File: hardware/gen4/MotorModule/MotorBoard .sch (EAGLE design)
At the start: 64 parts, among them IC1 XMEGA16A4A, M1O1 TEST_PT, M1O2 TEST_PT, M1O3 TEST_PT

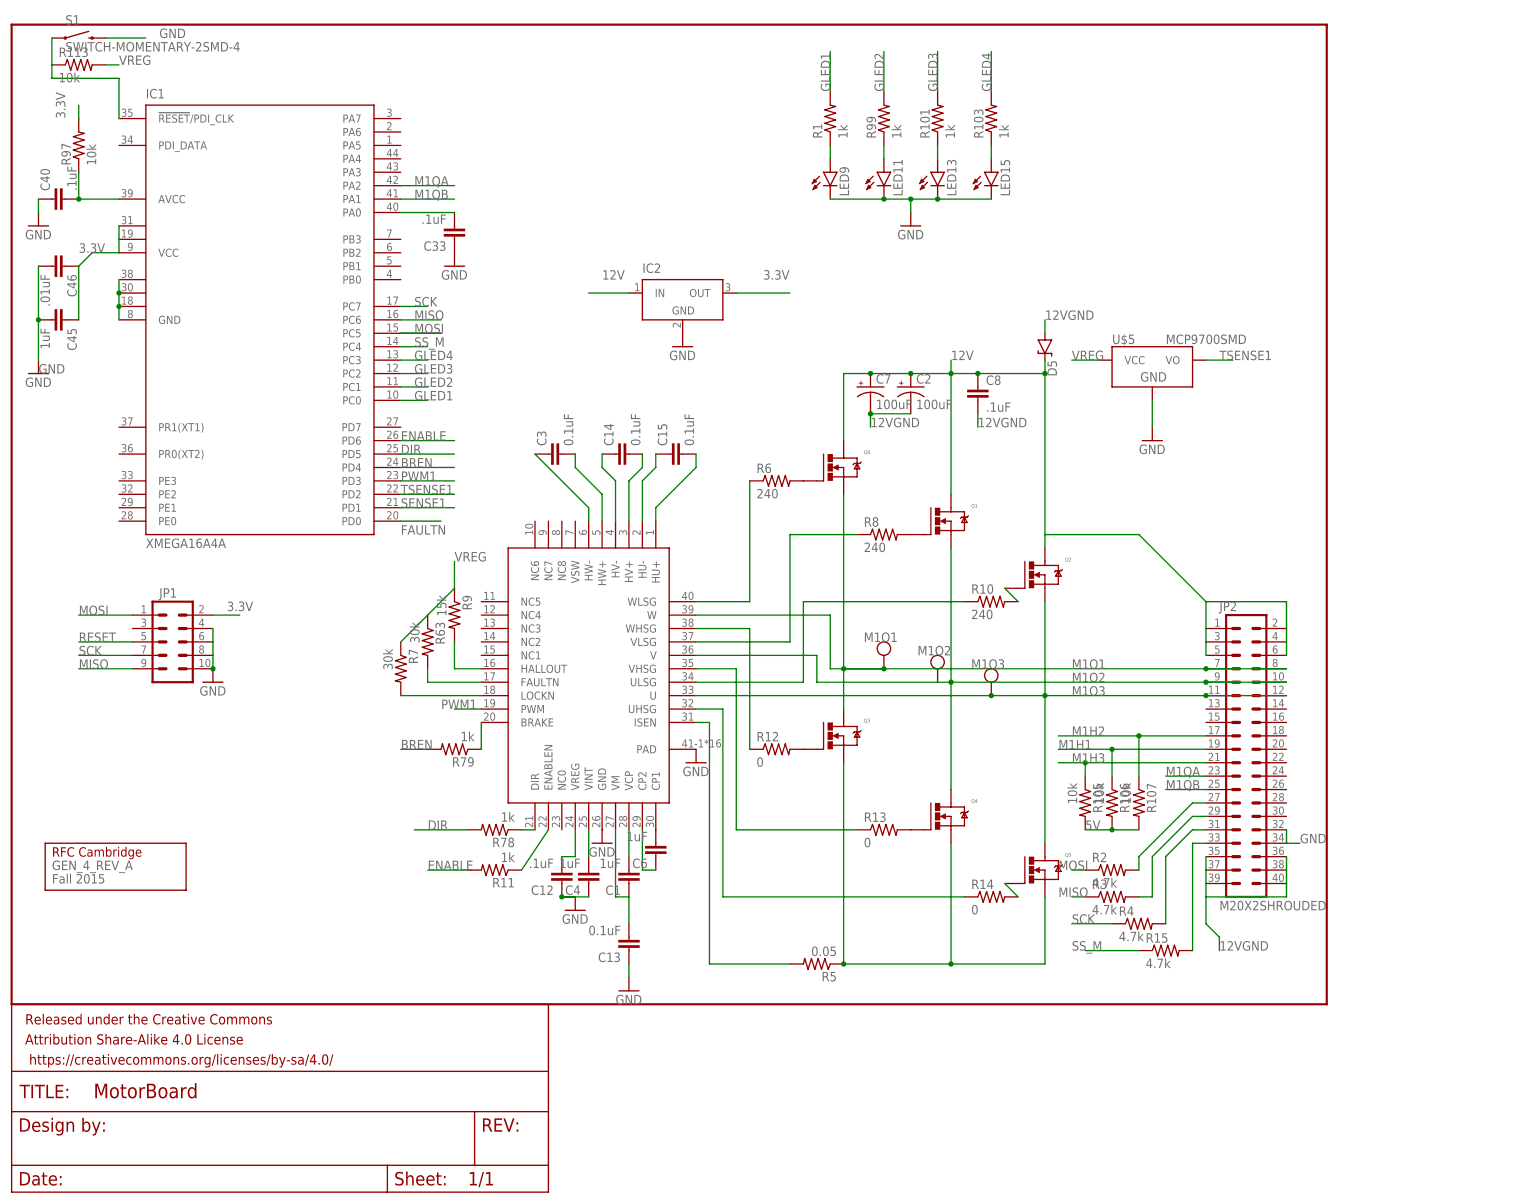
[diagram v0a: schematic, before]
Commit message: mother and motor board touchups
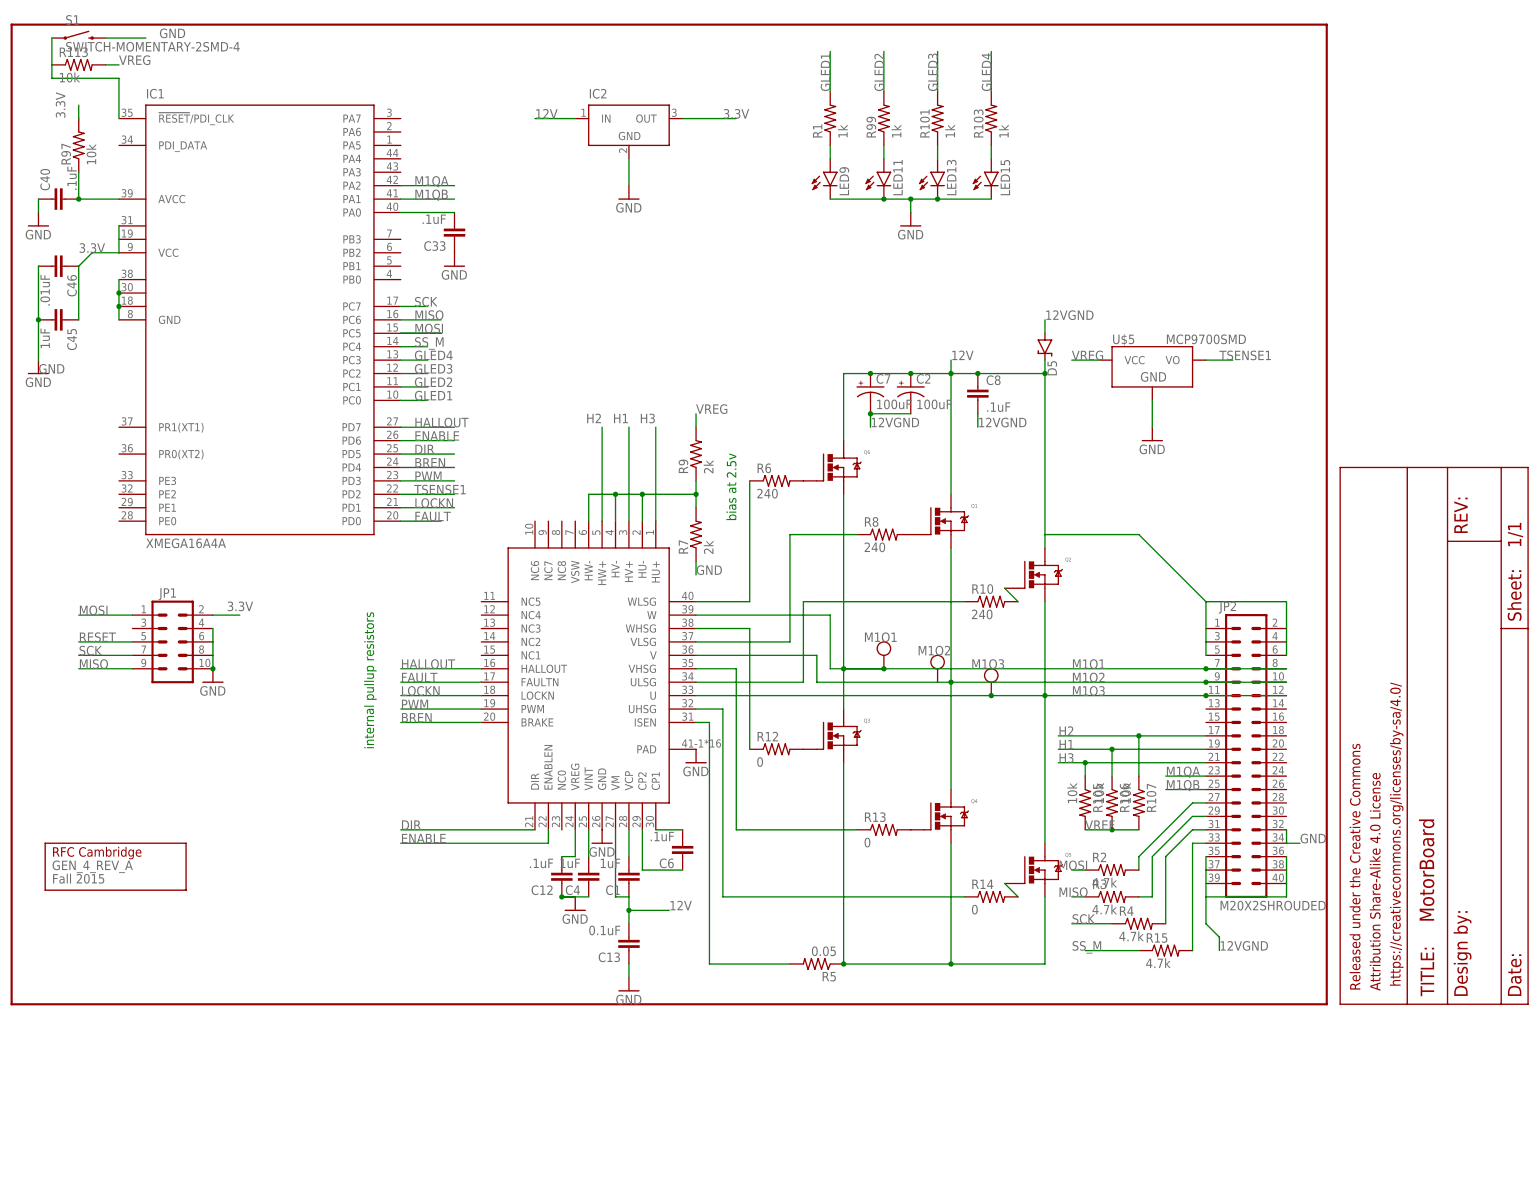
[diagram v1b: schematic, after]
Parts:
- removed C14, C15, C3: 0.1uF, SparkFun-Passives:CAP0805
- removed R11, R78, R79: 1k, SparkFun-Resistors:RESISTOR0805-RES
- removed R63: 30k, SparkFun-Resistors:RESISTOR0805-RES
- C6: value 1uF -> .1uF
- R7: value 30k -> 2k
- R9: value 15k -> 2k
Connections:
- net 5V renamed VREF
- net PWM1 renamed PWM
- removed net FAULT1: IC1.PD0
- removed net M1H1: JP2.19, R106.1
- removed net M1H2: JP2.17, R107.1
- removed net M1H3: JP2.21, R105.1
- removed net N$22: C3.1, U$1.HW-
- removed net N$23: R79.1, U$1.BRAKE
- removed net N$24: R7.2, U$1.LOCKN
- removed net N$25: C3.2, U$1.HW+
- removed net N$26: C14.1, U$1.HV-
- removed net N$27: C14.2, U$1.HV+
- removed net N$28: R63.2, U$1.FAULTN
- removed net N$30: C15.2, U$1.HU+
- removed net N$31: R9.2, U$1.HALLOUT
- removed net N$32: R11.1, U$1.ENABLEN
- removed net N$98: R78.1, U$1.DIR
- removed net SENSE1: IC1.PD1
- new net FAULT: IC1.PD0, U$1.FAULTN
- new net H1: JP2.19, R106.1, U$1.HV+
- new net H2: JP2.17, R107.1, U$1.HW+
- new net H3: JP2.21, R105.1, U$1.HU+
- new net HALLOUT: IC1.PD7, U$1.HALLOUT
- new net LOCKN: IC1.PD1, U$1.LOCKN
- net BREN: now also U$1.BRAKE; no longer R79.2
- net DIR: now also U$1.DIR; no longer R78.2
- net ENABLE: now also U$1.ENABLEN; no longer R11.2
- net GND: now also R7.1
- net N$29: now also R7.2, R9.1, U$1.HV-, U$1.HW-; no longer C15.1
- net VREG: now also R9.2; no longer R63.1, R7.1, R9.1
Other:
- note added: "bias at 2.5v"
- note added: "internal pullup resistors"
- note removed: "FAULTN"
- note removed: "SENSE1"
- note removed: "TSENSE1"
- moved on the sheet: C6, IC2, R7, R9

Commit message: some motor board stuff
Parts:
- removed IC2: (no value), linear-technology:LT1129CST5
- removed M1O1, M1O2, M1O3: TEST_PT, gen3:TEST_PT
- added 3.3REG: 3.3REG1AREG, gen3:3.3REG1AREG
- added 3.3V, O1, O2, O3: TEST_PT, gen3:TEST_PT
- added C10: 47uF, SparkFun-Capacitors:CAP1206
- added C3: 1uF, SparkFun-Capacitors:CAP0805
- added C5: .01uF, SparkFun-Capacitors:CAP0805
- added FRAME1: FRAME-LETTER, SparkFun-Aesthetics:FRAME-LETTER
- added PW_LED: (no value), SparkFun-LED:LED1206
- added RSENSE: .05, SparkFun-Resistors:RESISTOR0805-RES
- R5: value 0.05 -> 1k; device SparkFun-Resistors:RESISTOR0805-RES -> SparkFun-Passives:RESISTOR0805-RES
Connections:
- net TSENSE1 renamed TSENSE
- removed net M1O1: JP2.7, JP2.8, M1O1.P$1, Q3.P$1, Q6.P$2, U$1.W
- removed net M1O2: JP2.10, JP2.9, M1O2.P$1, Q1.P$2, Q4.P$1, U$1.V
- removed net M1O3: JP2.11, JP2.12, M1O3.P$1, Q2.P$2, Q5.P$1, U$1.U
- new net BOT: Q3.P$2, Q4.P$2, Q5.P$2, RSENSE.2, U$1.ISEN
- new net O2: JP2.10, JP2.9, O2.P$1, Q1.P$2, Q4.P$1, U$1.V
- new net O3: JP2.11, JP2.12, O3.P$1, Q2.P$2, Q5.P$1, U$1.U
- net 12V: now also 3.3REG.IN; no longer IC2G$1.IN
- net 12VGND: now also RSENSE.1
- net 3.3V: now also 3.3REG.OUT, 3.3V.P$1, C10.1, C3.1, C5.1, PW_LED.A, U$5.VCC; no longer IC2G$1.OUT
- net GND: now also 3.3REG.GND, C10.2, C3.2, C5.2, R5.1; no longer IC2G$1.GND
- net MISO: now also JP1.9
- net N$2: now also C6.1; no longer C6.2
- net N$5: now also PW_LED.C; no longer U$1.ISEN
- net N$9: now also C6.2; no longer C6.1
- net O1: now also JP2.7, JP2.8, O1.P$1, Q3.P$1, Q6.P$2, U$1.W; no longer Q3.P$2, Q4.P$2, Q5.P$2, R5.1
- net VREG: no longer U$5.VCC
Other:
- note added: "analog output temp sense"
- note added: "bias HALLs at 2.5v"
- note removed: "bias at 2.5v"
- moved on the sheet: C1, C12, C13, C2, C33, C4, C40, C45, C46, C6, C7, C8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
